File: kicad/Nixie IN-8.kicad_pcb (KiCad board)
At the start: 2 copper layers, 114.3 x 73.7 mm, 54 parts, among them J1 HOURS, J10 DOT, J2 MINUTES, J3 DOT, J4 Conn_01x03_Pin, J5 Conn_01x03_Pin, J6 Conn_01x02_Pin, J7 Barrel_Jack_Switch, J8 HOURS, J9 MINUTES, Q1 MPSA42, SW1 SW_SPST, SW2 SW_SPST, SW3 SW_SPST, U1 K155ID1, U2 K155ID1, U3 K155ID1, U4 K155ID1, U5 MCP7940N-xP, U6 74HC595, U7 74HC595, Y1 32.768kHz

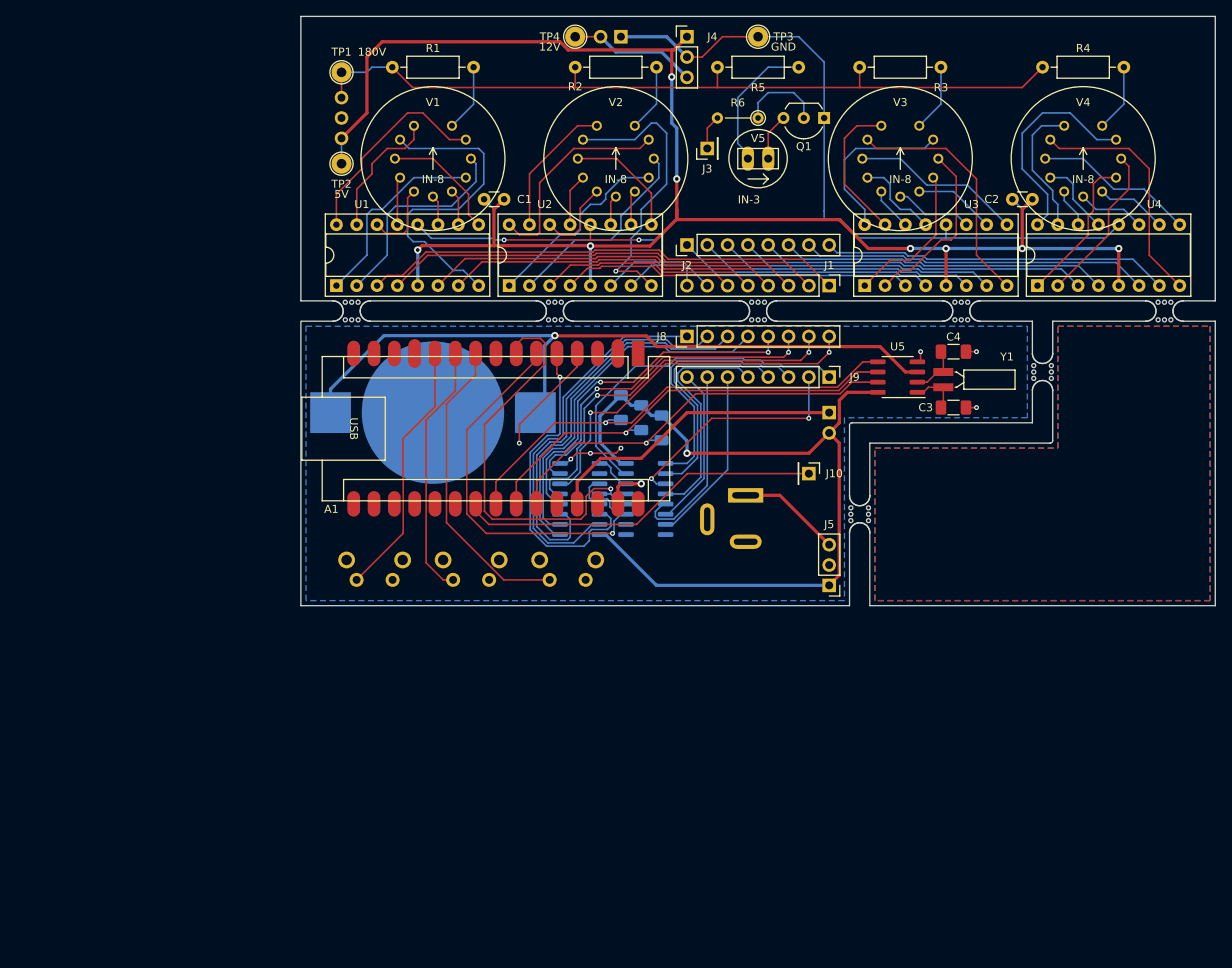
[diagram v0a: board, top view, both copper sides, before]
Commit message: removed backups
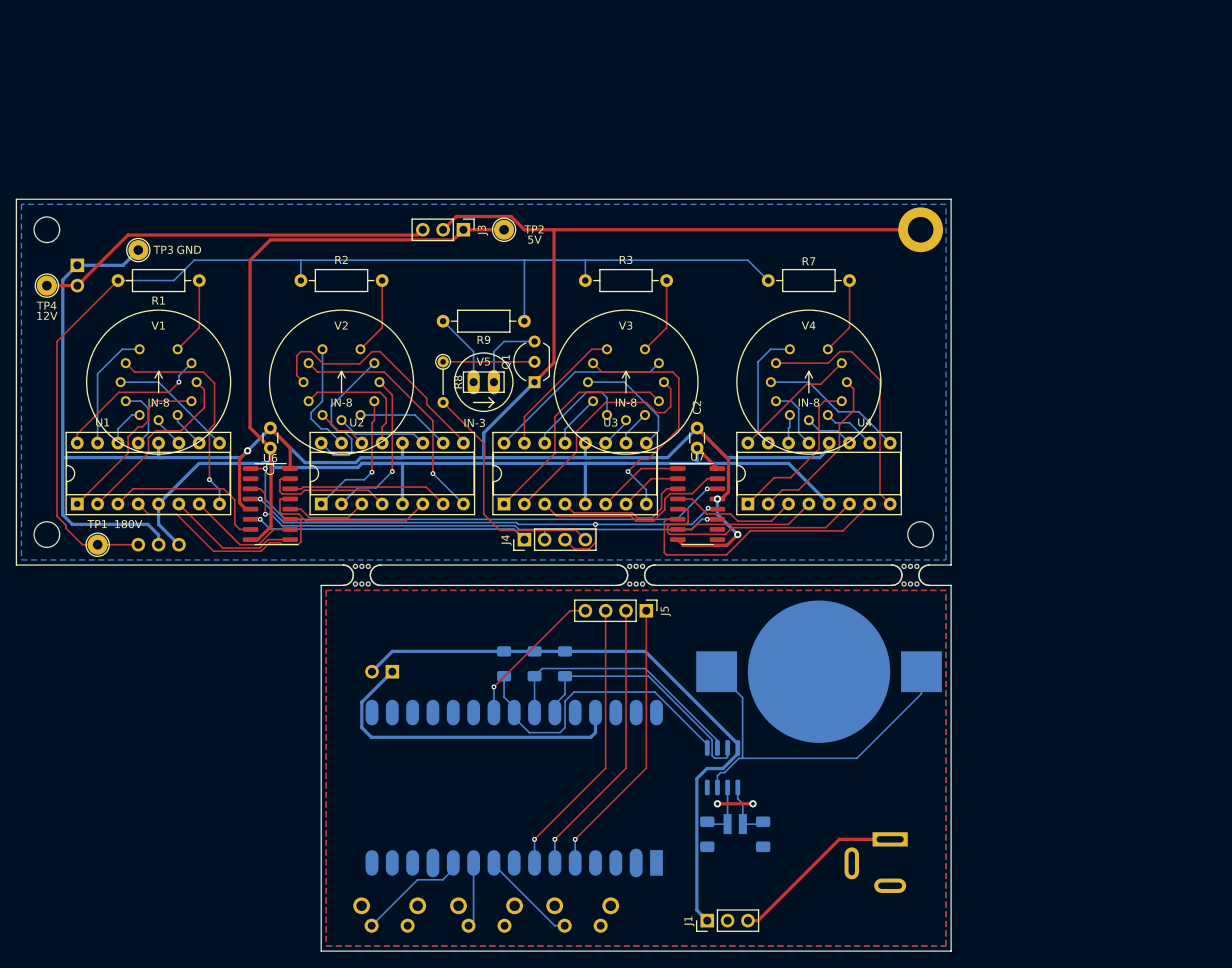
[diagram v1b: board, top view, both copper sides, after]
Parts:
- removed J10: DOT, Connector_PinHeader_2.54mm:PinHeader_1x01_P2.54mm_Vertical
- removed J7: Barrel_Jack_Switch, Connector_BarrelJack:BarrelJack_Wuerth_6941xx301002
- removed J8: HOURS, Connector_PinHeader_2.54mm:PinHeader_1x08_P2.54mm_Vertical
- removed J9: MINUTES, Connector_PinHeader_2.54mm:PinHeader_1x08_P2.54mm_Vertical
- removed the mouse-bite-2.54mm-slot at (219.7, 57.1)
- removed the mouse-bite-2.54mm-slot at (204.5, 64.8)
- removed the mouse-bite-2.54mm-slot at (168.9, 57.1)
- removed the mouse-bite-2.54mm-slot at (181.6, 82.5)
- removed the mouse-bite-2.54mm-slot at (194.3, 57.1)
- removed the mouse-bite-2.54mm-slot at (118.1, 57.1)
- removed the mouse-bite-2.54mm-slot at (143.5, 57.1)
- added REF**: MountingHole_3.2mm_M3_DIN965_Pad, MountingHole:MountingHole_3.2mm_M3_DIN965_Pad, F.Cu at (189.2, 47.0)
- added mouse-bite-2.54mm-slot: VAL**, Panelization:mouse-bite-2.54mm-slot, F.Cu at (188.0, 90.2)
- added mouse-bite-2.54mm-slot: VAL**, Panelization:mouse-bite-2.54mm-slot, F.Cu at (119.4, 90.2)
- added mouse-bite-2.54mm-slot: VAL**, Panelization:mouse-bite-2.54mm-slot, F.Cu at (153.7, 90.2)
- A1, C3, C4, U5, Y1: moved to B.Cu
- J1: value HOURS -> Conn_01x03_Pin; footprint Connector_PinHeader_2.54mm:PinHeader_1x08_P2.54mm_Vertical -> Connector_PinHeader_2.54mm:PinHeader_1x03_P2.54mm_Vertical
- J2: value MINUTES -> Conn_01x02_Pin; footprint Connector_PinHeader_2.54mm:PinHeader_1x08_P2.54mm_Vertical -> Connector_PinHeader_2.54mm:PinHeader_1x02_P2.54mm_Horizontal; moved to B.Cu
- J3: value DOT -> Conn_01x03_Pin; footprint Connector_PinHeader_2.54mm:PinHeader_1x01_P2.54mm_Vertical -> Connector_PinHeader_2.54mm:PinHeader_1x03_P2.54mm_Vertical
- J4, J5: value Conn_01x03_Pin -> Conn_01x04_Pin; footprint Connector_PinHeader_2.54mm:PinHeader_1x03_P2.54mm_Vertical -> Connector_PinHeader_2.54mm:PinHeader_1x04_P2.54mm_Vertical
- J6: value Conn_01x02_Pin -> Barrel_Jack_Switch; footprint Connector_PinHeader_2.54mm:PinHeader_1x02_P2.54mm_Horizontal -> Connector_BarrelJack:BarrelJack_Wuerth_6941xx301002
- R4: value 12k -> 10k; footprint Resistor_THT:R_Axial_DIN0207_L6.3mm_D2.5mm_P10.16mm_Horizontal -> Resistor_SMD:R_1206_3216Metric_Pad1.30x1.75mm_HandSolder; moved to B.Cu
- R5: value 200k -> 10k; footprint Resistor_THT:R_Axial_DIN0207_L6.3mm_D2.5mm_P10.16mm_Horizontal -> Resistor_SMD:R_1206_3216Metric_Pad1.30x1.75mm_HandSolder; moved to B.Cu
- R6: value 13.5k -> 10k; footprint Resistor_THT:R_Axial_DIN0204_L3.6mm_D1.6mm_P5.08mm_Vertical -> Resistor_SMD:R_1206_3216Metric_Pad1.30x1.75mm_HandSolder; moved to B.Cu
- R7: value 10k -> 12k; footprint Resistor_SMD:R_1206_3216Metric_Pad1.30x1.75mm_HandSolder -> Resistor_THT:R_Axial_DIN0207_L6.3mm_D2.5mm_P10.16mm_Horizontal; moved to F.Cu
- R8: value 10k -> 13.5k; footprint Resistor_SMD:R_1206_3216Metric_Pad1.30x1.75mm_HandSolder -> Resistor_THT:R_Axial_DIN0204_L3.6mm_D1.6mm_P5.08mm_Vertical; moved to F.Cu
- R9: value 10k -> 200k; footprint Resistor_SMD:R_1206_3216Metric_Pad1.30x1.75mm_HandSolder -> Resistor_THT:R_Axial_DIN0207_L6.3mm_D2.5mm_P10.16mm_Horizontal; moved to F.Cu
- U6, U7: moved to F.Cu
- moved R4 97.9 mm to (141.0, 101.2), turned to -90 degrees
- moved TP3 81.9 mm to (91.4, 49.5)
- moved J1 80.8 mm to (162.6, 133.3), turned to 90 degrees
- moved R5 79.2 mm to (137.2, 101.2), turned to -90 degrees
- moved TP4 73.0 mm to (80.0, 54.0)
- moved R6 72.4 mm to (144.8, 101.2), turned to -90 degrees
- moved C4 67.7 mm to (162.6, 122.6), turned to -90 degrees
- moved TP1 66.5 mm to (86.4, 86.4)
- moved J4 66.1 mm to (139.7, 85.7), turned to 90 degrees
- moved J2 64.8 mm to (123.2, 102.2)
- moved Y1 61.1 mm to (167.0, 122.0), turned to 180 degrees
- moved A1 60.2 mm to (156.2, 124.4), turned to 90 degrees
- moved C3 58.4 mm to (169.5, 122.6), turned to -90 degrees
- moved BT1 58.1 mm to (176.5, 102.2)
- moved VR1 57.6 mm to (91.4, 67.9), turned to -90 degrees
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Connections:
- A1 pad 5: /DATA -> /MCU_DATA
- A1 pad 6: /CLOCK -> /MCU_CLOCK
- A1 pad 7: /LATCH -> /MCU_LATCH
- J1 pad 1: /HOUR1.A -> /5V_2
- J1 pad 2: /HOUR1.D -> GND2
- J1 pad 3: /HOUR1.B -> /12V_2
- J2 pad 1: /MINUTE1.A -> Net-(A1-+5V)
- J2 pad 2: /MINUTE1.D -> /5V_2
- J3 pad 1: /DOT -> /5V_1
- J4 pad 1: /5V_1 -> /DATA
- J4 pad 2: GND1 -> /CLOCK
- J4 pad 3: /12V_1 -> /LATCH
- J5 pad 1: /5V_2 -> /MCU_DATA
- J5 pad 2: GND2 -> /MCU_CLOCK
- J5 pad 3: /12V_2 -> /MCU_LATCH
- J6 pad 1: Net-(A1-+5V) -> /12V_2
- J6 pad 2: /5V_2 -> GND2
- R4 pad 1: /180V -> /5V_2
- R4 pad 2: Net-(R4-Pad2) -> /SCL
- R5 pad 1: /180V -> /5V_2
- R5 pad 2: Net-(R5-Pad2) -> /SDA
- R6 pad 1: Net-(Q1-B) -> /5V_2
- R6 pad 2: /DOT -> /MFP
- R7 pad 1: /5V_2 -> /180V
- R7 pad 2: /SCL -> Net-(R7-Pad2)
- R8 pad 1: /5V_2 -> Net-(Q1-B)
- R8 pad 2: /SDA -> /DOT
- R9 pad 1: /5V_2 -> /180V
- R9 pad 2: /MFP -> Net-(R9-Pad2)
- U6 pad 1: /MCU_HOUR1.B -> /HOUR1.B
- U6 pad 13: GND2 -> GND1
- U6 pad 15: /MCU_HOUR1.A -> /HOUR1.A
- U6 pad 16: /5V_2 -> /5V_1
- U6 pad 2: /MCU_HOUR1.C -> /HOUR1.C
- U6 pad 3: /MCU_HOUR1.D -> /HOUR1.D
- U6 pad 4: /MCU_HOUR2.A -> /HOUR2.A
- U6 pad 5: /MCU_HOUR2.B -> /HOUR2.B
- U6 pad 6: /MCU_HOUR2.C -> /HOUR2.C
- U6 pad 7: /MCU_HOUR2.D -> /HOUR2.D
- U6 pad 8: GND2 -> GND1
- U7 pad 1: /MCU_MINUTE1.B -> /MINUTE1.B
- U7 pad 13: GND2 -> GND1
- U7 pad 15: /MCU_MINUTE1.A -> /MINUTE1.A
- U7 pad 16: /5V_2 -> /5V_1
- U7 pad 2: /MCU_MINUTE1.C -> /MINUTE1.C
- U7 pad 3: /MCU_MINUTE1.D -> /MINUTE1.D
- U7 pad 4: /MCU_MINUTE2.A -> /MINUTE2.A
- U7 pad 5: /MCU_MINUTE2.B -> /MINUTE2.B
- U7 pad 6: /MCU_MINUTE2.C -> /MINUTE2.C
- U7 pad 7: /MCU_MINUTE2.D -> /MINUTE2.D
- U7 pad 8: GND2 -> GND1
- V4 pad A: Net-(R4-Pad2) -> Net-(R7-Pad2)
- V5 pad A: Net-(R5-Pad2) -> Net-(R9-Pad2)
- VR1 pad 4: GND -> GND1
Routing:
- net GND1: track 153.9 -> 298.8 mm, vias 2 -> 3
- net Net-(U6-QH'): track 4.71 -> 64.8 mm, vias 0 -> 2
- net /MCU_HOUR1.D: track 48.5 -> 0.00 mm
- net /MCU_HOUR2.B: track 47.5 -> 0.00 mm, vias 2 -> 0
- net /MCU_HOUR1.A: track 47.3 -> 0.00 mm
- net /MCU_HOUR2.C: track 46.1 -> 0.00 mm, vias 2 -> 0
- net Net-(BT1-+): track 91.6 -> 46.1 mm, vias 1 -> 0
- net /MCU_HOUR1.C: track 45.1 -> 0.00 mm
- net /MCU_HOUR2.A: track 44.5 -> 0.00 mm, vias 2 -> 0
- net /MCU_HOUR1.B: track 44.2 -> 0.00 mm
- net /MCU_MINUTE1.A: track 42.9 -> 0.00 mm
- net /MCU_HOUR2.D: track 42.6 -> 0.00 mm, vias 2 -> 0
- net /180V: track 100.8 -> 140.6 mm
- net /HOUR1.A: track 60.2 -> 21.3 mm
- net /MCU_LATCH: track 0.00 -> 35.2 mm, vias 0 -> 1
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- added copper zone on B.Cu, net (none)
- added copper zone on F.Cu, net (none)
- removed copper zone on B.Cu, net GND
- removed copper zone on F.Cu, net GND
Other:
- board size 114.3 x 73.7 mm -> 116.8 x 94 mm

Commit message: updated pcb
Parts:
- removed mouse-bite-2.54mm-slot (x3): VAL**, Panelization:mouse-bite-2.54mm-slot
- added mouse-bite-2.54mm-slot1: VAL**, Panelization:mouse-bite-2.54mm-slot, F.Cu at (120.7, 90.2)
- added mouse-bite-2.54mm-slot2: VAL**, Panelization:mouse-bite-2.54mm-slot, F.Cu at (154.3, 90.2)
- added mouse-bite-2.54mm-slot3: VAL**, Panelization:mouse-bite-2.54mm-slot, F.Cu at (188.0, 90.2)
- A1: value Arduino_Nano_Every -> ARDUINO NANO EVERY
- BT1: value Battery_Cell -> CR2032
- R8: value 13.5k -> 22k
- TP1: value TPHV -> 180V
- TP2: value TP5V -> 5V
- TP3: value TPGND -> GND
- TP4: value TP12V -> 12V
- U5: value MCP7940N-xP -> MCP7940N
- moved Q1 7.96 mm to (137.2, 59.1), turned to 180 degrees
- moved R9 5.08 mm to (139.7, 53.3)
- moved J6 3.07 mm to (186.7, 120.4)
- moved SW3 2.86 mm to (121.9, 131.4)
- moved SW2 2.84 mm to (134.0, 131.4)
- moved SW1 2.84 mm to (146.0, 131.4)
- moved R1 1.91 mm to (90.8, 53.3)
- moved R7 1.91 mm to (168.3, 53.3)
- moved V1 1.91 mm to (95.9, 66.0)
- moved V4 1.91 mm to (173.4, 66.0)
- moved VR1 1.90 mm to (91.4, 66.0)
- moved C3 1.80 mm to (170.8, 121.3)
- moved C4 1.80 mm to (163.8, 121.3)
- moved R4 1.80 mm to (142.2, 100.0)
- moved R5 1.80 mm to (138.4, 100.0)
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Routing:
- net GND1: track 298.8 -> 318.4 mm
- net Net-(U4-0): track 15.9 -> 27.5 mm
- net Net-(U2-3): track 31.3 -> 21.9 mm
- net Net-(U3-2): track 31.4 -> 23.3 mm
- net Net-(U1-0): track 20.2 -> 27.5 mm, vias 1 -> 0
- net Net-(R9-Pad2): track 9.20 -> 14.3 mm
- net Net-(U2-4): track 16.3 -> 11.3 mm
- net Net-(U4-3): track 18.1 -> 22.5 mm
- net /5V_2: track 77.5 -> 81.7 mm
- net Net-(Q1-B): track 11.4 -> 7.67 mm
- net GND2: track 4.44 -> 8.19 mm
- net Net-(U1-9): track 23.0 -> 26.7 mm
- net /180V: track 140.6 -> 137.0 mm
- net Net-(U2-1): track 14.3 -> 17.3 mm
- net Net-(U4-1): track 15.3 -> 12.7 mm
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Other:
- board size 116.8 x 94 mm -> 116.8 x 91.4 mm
- board text added: "HIGH VOLTAGE! DANGER!"
- board text added: "JLCJLCJLCJLC"
- board text added: "NIXIE IN-8"
- board text added: "R3.0"
- board text added: "ZENO GRIES"
- board text removed: "12V"
- board text removed: "180V"
- board text removed: "5V"
- board text removed: "GND"

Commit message: added partslist
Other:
- rule pad_to_mask_clearance: 0.0508 -> 0
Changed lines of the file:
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@@
       (dielectric_constraints no)
     )
-    (pad_to_mask_clearance 0.0508)
+    (pad_to_mask_clearance 0)
     (pcbplotparams
       (layerselection 0x00010fc_ffffffff)
       (plot_on_all_layers_selection 0x0000000_00000000)
       (disableapertmacros false)
-      (usegerberextensions false)
-      (usegerberattributes true)
-      (usegerberadvancedattributes true)
-      (creategerberjobfile true)
+      (usegerberextensions true)
+      (usegerberattributes false)
+      (usegerberadvancedattributes false)
+      (creategerberjobfile false)
       (dashed_line_dash_ratio 12.000000)
       (dashed_line_gap_ratio 3.000000)
@@
       (plotinvisibletext false)
       (sketchpadsonfab false)
-      (subtractmaskfromsilk false)
+      (subtractmaskfromsilk true)
       (outputformat 1)
       (mirror false)
-      (drillshape 1)
+      (drillshape 0)
       (scaleselection 1)
-      (outputdirectory "")
+      (outputdirectory "gerber/")
     )
   )
@@
     (fp_line (start 1.6 0.8) (end 1.6 -0.8)
       (stroke (width 0.1) (type solid)) (layer "B.Fab"))
-    (pad "1" smd roundrect (at -1.55 0 270) (size 1.3 1.75) (layers "B.Cu" "B.Paste" "B.Mask") (roundrect_rratio 0.192308)
+    (pad "1" smd roundrect (at -1.55 0 270) (size 1.3 1.75) (layers "B.Cu" "B.Paste" "B.Mask") (roundrect_rratio 0.1923076923)
       (net 97 "/5V_2") (pintype "passive"))
-    (pad "2" smd roundrect (at 1.55 0 270) (size 1.3 1.75) (layers "B.Cu" "B.Paste" "B.Mask") (roundrect_rratio 0.192308)
+    (pad "2" smd roundrect (at 1.55 0 270) (size 1.3 1.75) (layers "B.Cu" "B.Paste" "B.Mask") (roundrect_rratio 0.1923076923)
       (net 11 "/SDA") (pintype "passive"))
     (model "${KICAD6_3DMODEL_DIR}/Resistor_SMD.3dshapes/R_1206_3216Metric.wrl"
@@
     (fp_line (start 1.6 0.8) (end 1.6 -0.8)
       (stroke (width 0.1) (type solid)) (layer "B.Fab"))
-    (pad "1" smd roundrect (at -1.55 0 270) (size 1.3 1.75) (layers "B.Cu" "B.Paste" "B.Mask") (roundrect_rratio 0.192308)
+    (pad "1" smd roundrect (at -1.55 0 270) (size 1.3 1.75) (layers "B.Cu" "B.Paste" "B.Mask") (roundrect_rratio 0.1923076923)
       (net 97 "/5V_2") (pintype "passive"))
-    (pad "2" smd roundrect (at 1.55 0 270) (size 1.3 1.75) (layers "B.Cu" "B.Paste" "B.Mask") (roundrect_rratio 0.192308)
+    (pad "2" smd roundrect (at 1.55 0 270) (size 1.3 1.75) (layers "B.Cu" "B.Paste" "B.Mask") (roundrect_rratio 0.1923076923)
       (net 12 "/SCL") (pintype "passive"))
     (model "${KICAD6_3DMODEL_DIR}/Resistor_SMD.3dshapes/R_1206_3216Metric.wrl"
@@
     (fp_line (start 1.6 0.8) (end 1.6 -0.8)
       (stroke (width 0.1) (type solid)) (layer "B.Fab"))
-    (pad "1" smd roundrect (at -1.5625 0 270) (size 1.325 1.8) (layers "B.Cu" "B.Paste" "B.Mask") (roundrect_rratio 0.188679)
+    (pad "1" smd roundrect (at -1.5625 0 270) (size 1.325 1.8) (layers "B.Cu" "B.Paste" "B.Mask") (roundrect_rratio 0.1886792453)
       (net 4 "Net-(U5-X2)") (pintype "passive"))
-    (pad "2" smd roundrect (at 1.5625 0 270) (size 1.325 1.8) (layers "B.Cu" "B.Paste" "B.Mask") (roundrect_rratio 0.188679)
+    (pad "2" smd roundrect (at 1.5625 0 270) (size 1.325 1.8) (layers "B.Cu" "B.Paste" "B.Mask") (roundrect_rratio 0.1886792453)
       (net 92 "GND2") (pintype "passive"))
     (model "${KICAD6_3DMODEL_DIR}/Capacitor_SMD.3dshapes/C_1206_3216Metric.wrl"
@@
     (fp_line (start 1.6 0.8) (end 1.6 -0.8)
       (stroke (width 0.1) (type solid)) (layer "B.Fab"))
-    (pad "1" smd roundrect (at -1.5625 0 270) (size 1.325 1.8) (layers "B.Cu" "B.Paste" "B.Mask") (roundrect_rratio 0.188679)
+    (pad "1" smd roundrect (at -1.5625 0 270) (size 1.325 1.8) (layers "B.Cu" "B.Paste" "B.Mask") (roundrect_rratio 0.1886792453)
       (net 3 "Net-(U5-X1)") (pintype "passive"))
-    (pad "2" smd roundrect (at 1.5625 0 270) (size 1.325 1.8) (layers "B.Cu" "B.Paste" "B.Mask") (roundrect_rratio 0.188679)
+    (pad "2" smd roundrect (at 1.5625 0 270) (size 1.325 1.8) (layers "B.Cu" "B.Paste" "B.Mask") (roundrect_rratio 0.1886792453)
       (net 92 "GND2") (pintype "passive"))
     (model "${KICAD6_3DMODEL_DIR}/Capacitor_SMD.3dshapes/C_1206_3216Metric.wrl"
@@
     (fp_line (start 1.6 0.8) (end 1.6 -0.8)
       (stroke (width 0.1) (type solid)) (layer "B.Fab"))
-    (pad "1" smd roundrect (at -1.55 0 270) (size 1.3 1.75) (layers "B.Cu" "B.Paste" "B.Mask") (roundrect_rratio 0.192308)
+    (pad "1" smd roundrect (at -1.55 0 270) (size 1.3 1.75) (layers "B.Cu" "B.Paste" "B.Mask") (roundrect_rratio 0.1923076923)
       (net 97 "/5V_2") (pintype "passive"))
-    (pad "2" smd roundrect (at 1.55 0 270) (size 1.3 1.75) (layers "B.Cu" "B.Paste" "B.Mask") (roundrect_rratio 0.192308)
+    (pad "2" smd roundrect (at 1.55 0 270) (size 1.3 1.75) (layers "B.Cu" "B.Paste" "B.Mask") (roundrect_rratio 0.1923076923)
       (net 10 "/MFP") (pintype "passive"))
     (model "${KICAD6_3DMODEL_DIR}/Resistor_SMD.3dshapes/R_1206_3216Metric.wrl"
@@
     (effects (font (size 0.8 0.8) (thickness 0.1524) bold) (justify left bottom))
   )
-  (dimension (type aligned) (layer "User.1")
-    (pts (xy 114.3 137.16) (xy 114.3 91.44))
-    (height -3.175)
-    (gr_text "45,7200 mm" (at 109.975 114.3 90) (layer "User.1")
+  (dimension (type aligned) (layer "User.2")
+    (pts (xy 193.04 43.18) (xy 193.04 134.62))
+    (height -5.08)
+    (gr_text "91,4400 mm" (at 196.97 88.9 90) (layer "User.2")
       (effects (font (size 1 1) (thickness 0.15)))
     )
@@
   )
   (dimension (type aligned) (layer "User.2")
-    (pts (xy 193.04 137.16) (xy 193.04 43.18))
-    (height 3.81)
-    (gr_text "93,9800 mm" (at 195.7 90.17 90) (layer "User.2")
+    (pts (xy 76.2 43.18) (xy 193.04 43.18))
+    (height -5.08)
+    (gr_text "116,8400 mm" (at 134.62 36.95) (layer "User.2")
       (effects (font (size 1 1) (thickness 0.15)))
     )
@@
     (style (thickness 0.15) (arrow_length 1.27) (text_position_mode 0) (extension_height 0.58642) (extension_offset 0.5) keep_text_aligned)
   )
-  (dimension (type aligned) (layer "User.2")
-    (pts (xy 76.2 43.18) (xy 193.04 43.18))
-    (height -5.08)
-    (gr_text "116,8400 mm" (at 134.62 36.95) (layer "User.2")
+  (dimension (type aligned) (layer "User.3")
+    (pts (xy 115.57 134.62) (xy 193.04 134.62))
+    (height 2.539999)
+    (gr_text "77,4700 mm" (at 154.305 136.009999) (layer "User.3")
       (effects (font (size 1 1) (thickness 0.15)))
     )
@@
   )
   (dimension (type aligned) (layer "User.3")
-    (pts (xy 76.2 88.9) (xy 76.2 43.18))
-    (height -3.175)
-    (gr_text "45,7200 mm" (at 71.875 66.04 90) (layer "User.3")
+    (pts (xy 115.57 91.44) (xy 115.57 134.62))
+    (height 2.54)
+    (gr_text "43,1800 mm" (at 111.88 113.03 90) (layer "User.3")
       (effects (font (size 1 1) (thickness 0.15)))
     )
@@
   )
   (dimension (type aligned) (layer "User.3")
-    (pts (xy 114.3 137.16) (xy 193.04 137.16))
-    (height 3.174999)
-    (gr_text "78,7400 mm" (at 153.67 139.184999) (layer "User.3")
+    (pts (xy 115.57 91.44) (xy 115.57 88.9))
+    (height -5.08)
+    (gr_text "2,5400 mm" (at 108.585 93.345 90) (layer "User.3")
+      (effects (font (size 1 1) (thickness 0.15)))
+    )
+    (format (prefix "") (suffix "") (units 3) (units_format 1) (precision 4))
+    (style (thickness 0.15) (arrow_length 1.27) (text_position_mode 2) (extension_height 0.58642) (extension_offset 0.5) keep_text_aligned)
+  )
+  (dimension (type aligned) (layer "User.3")
+    (pts (xy 76.2 88.9) (xy 76.2 43.18))
+    (height -2.54)
+    (gr_text "45,7200 mm" (at 72.51 66.04 90) (layer "User.3")
+      (effects (font (size 1 1) (thickness 0.15)))
+    )
+    (format (prefix "") (suffix "") (units 3) (units_format 1) (precision 4))
+    (style (thickness 0.15) (arrow_length 1.27) (text_position_mode 0) (extension_height 0.58642) (extension_offset 0.5) keep_text_aligned)
+  )
+  (dimension (type aligned) (layer "User.4")
+    (pts (xy 95.885 66.04) (xy 95.885 43.18))
+    (height -29.21)
+    (gr_text "22,8600 mm" (at 65.525 54.61 90) (layer "User.4")
+      (effects (font (size 1 1) (thickness 0.15)))
+    )
+    (format (prefix "") (suffix "") (units 3) (units_format 1) (precision 4))
+    (style (thickness 0.15) (arrow_length 1.27) (text_position_mode 0) (extension_height 0.58642) (extension_offset 0.5) keep_text_aligned)
+  )
+  (dimension (type aligned) (layer "User.4")
+    (pts (xy 95.885 66.04) (xy 76.2 66.04))
+    (height 34.29)
+    (gr_text "19,6850 mm" (at 86.0425 30.6) (layer "User.4")
       (effects (font (size 1 1) (thickness 0.15)))
     )
